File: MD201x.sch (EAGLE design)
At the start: 103 parts, among them IC1 78L05F, IC2 LM321MF, J1 8P8C-LED, J4 MA04-2, J5 MA05-2, J6 MA02-2, Q1 N-MOSFET-, Q2 N-MOSFET-, Q3 N-MOSFET-, Q4 N-MOSFET-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

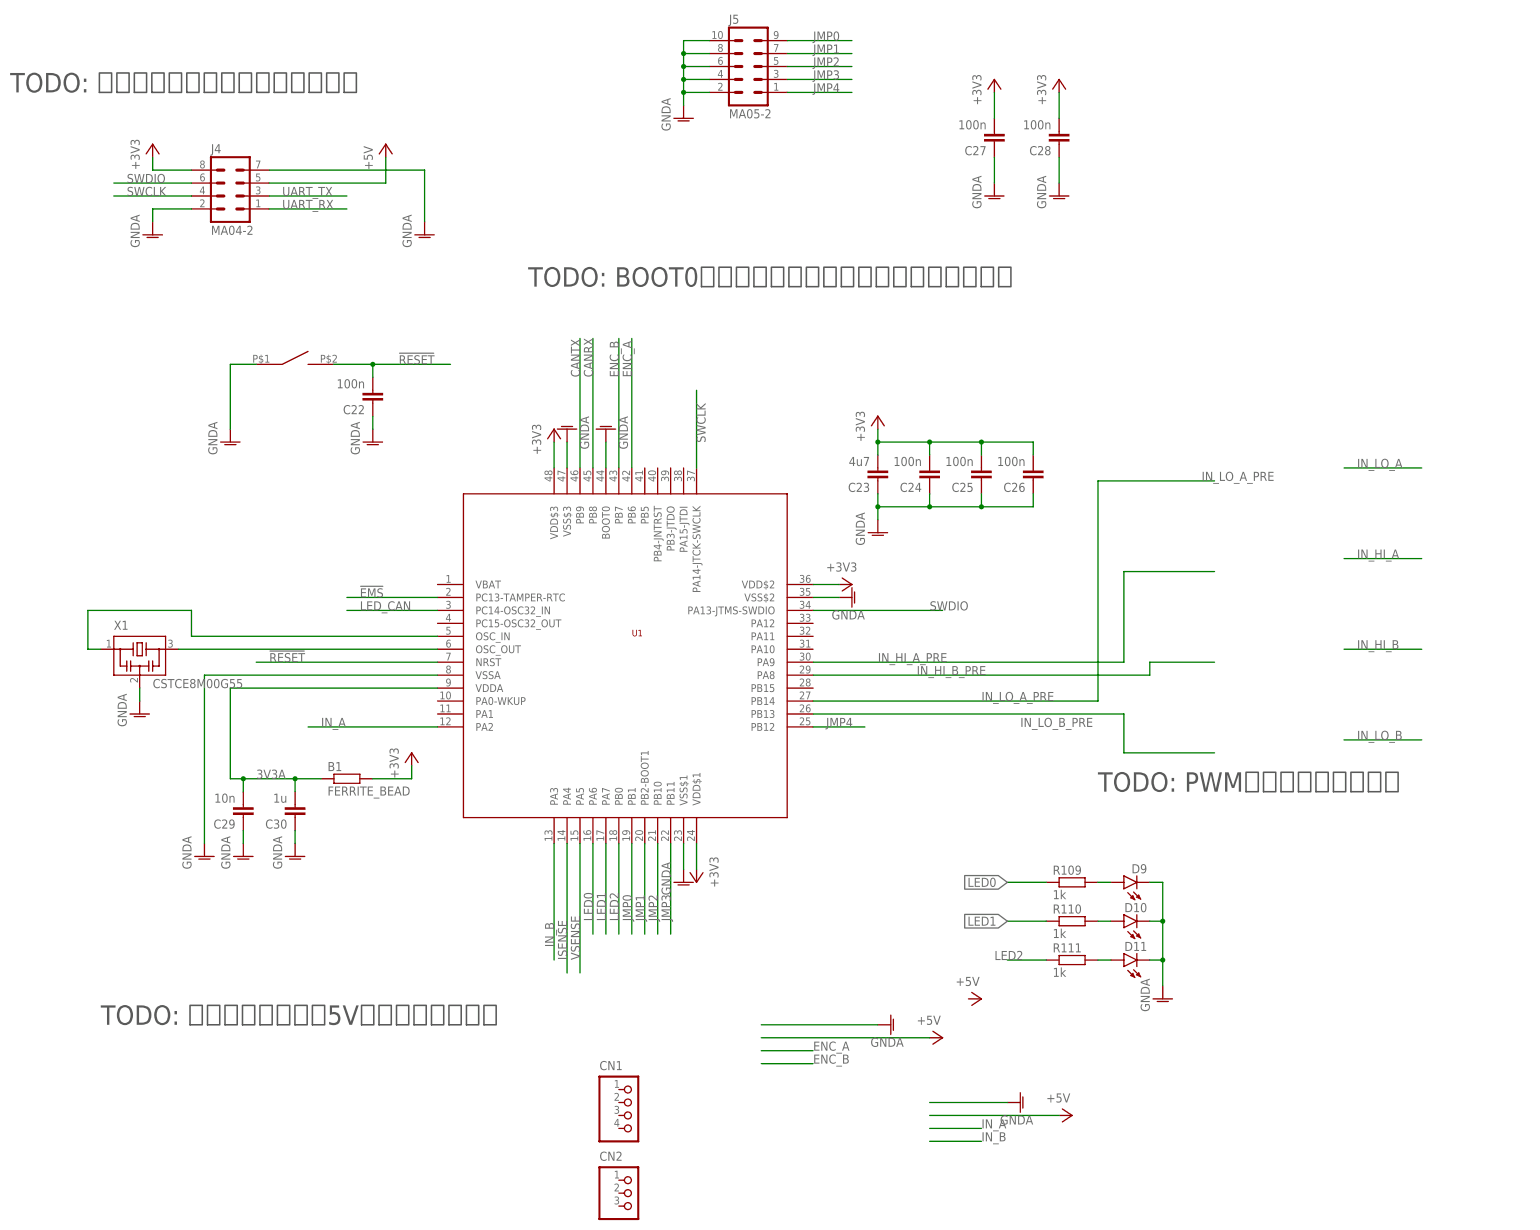
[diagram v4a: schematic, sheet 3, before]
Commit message: change: board size to 50x100, back-to-back MOSFETs
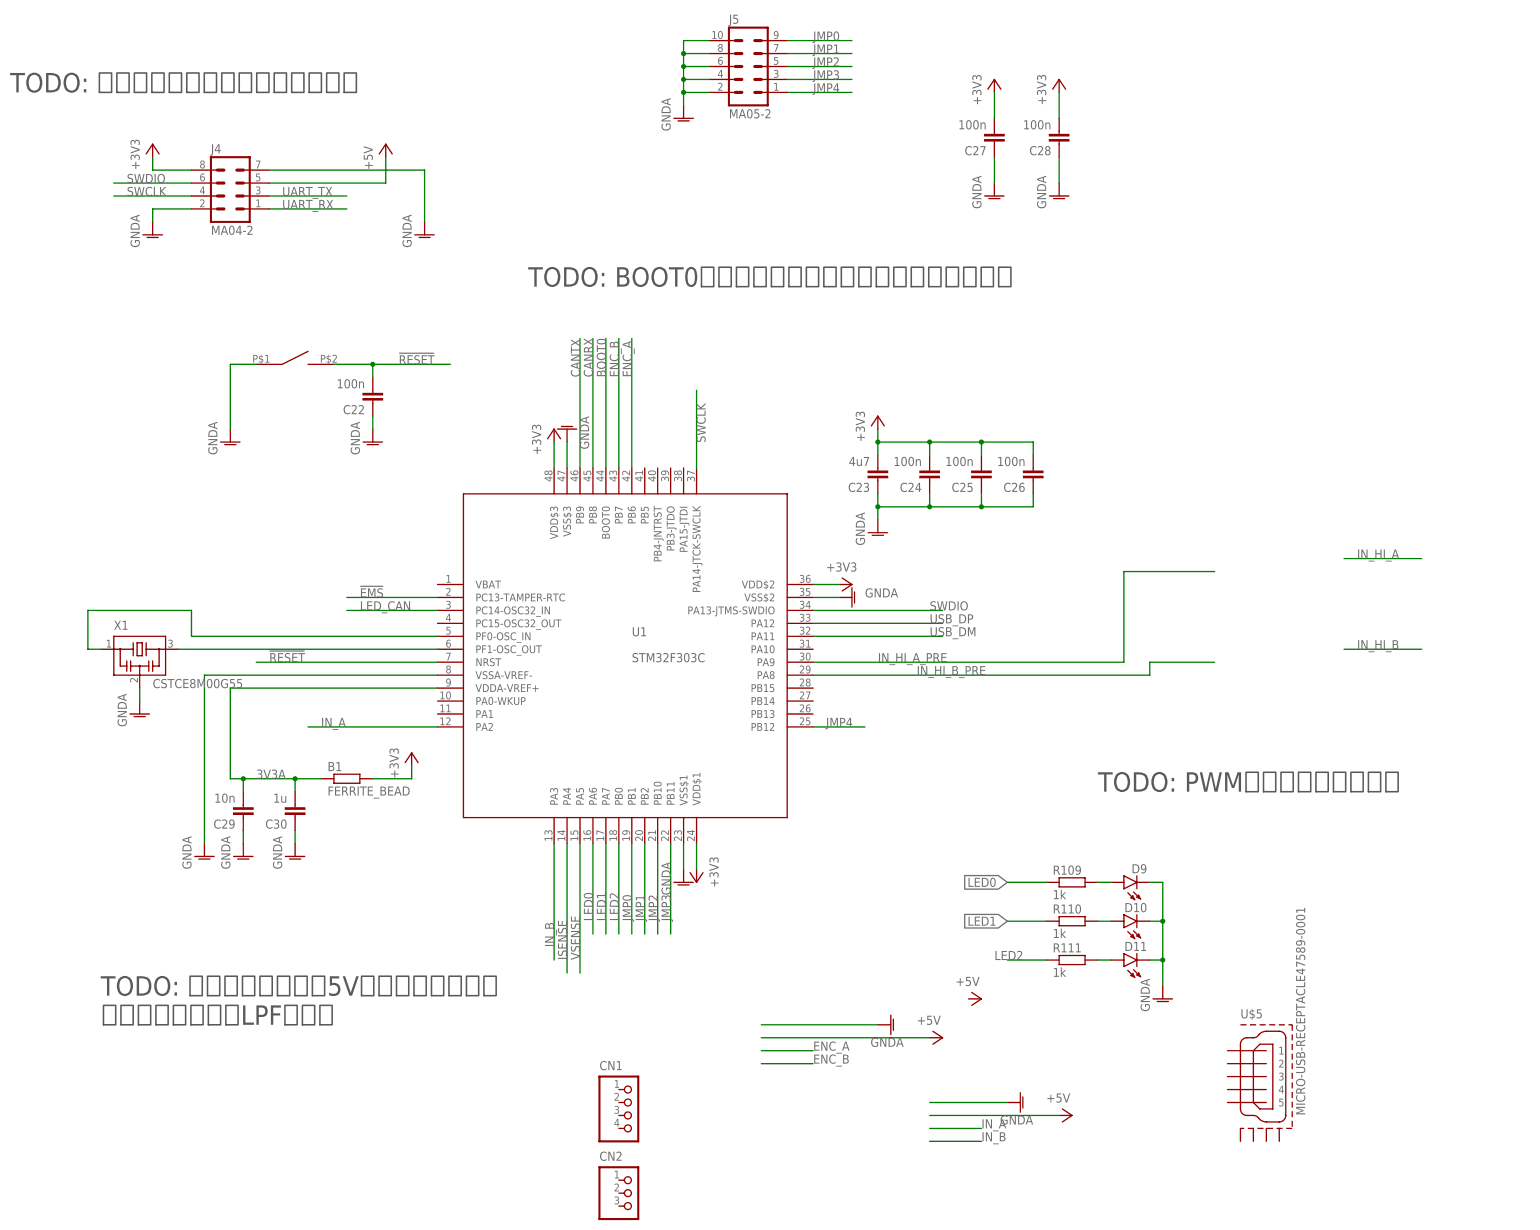
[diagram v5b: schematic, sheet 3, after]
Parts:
- added D4: BAS16W, diode:DIODE-SOD323-R
- added U$5: MICRO-USB-RECEPTACLE47589-0001, con-molex-usb:MICRO-USB-RECEPTACLE47589-0001
- U1: value STM32F103C8 -> STM32F303C; device stm32_mcu:STM32F103C8 -> stm32_mcu:STM32F303C
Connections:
- removed net IN_LO_A_PRE: U1.PB14
- removed net IN_LO_B_PRE: U1.PB13
- new net BOOT0: U1.BOOT0
- new net USB_DM: U1.PA11
- new net USB_DP: U1.PA12
- net 3V3A: now also U1.VDDA-VREF+; no longer U1.VDDA
- net GNDA: now also U1.VSSA-VREF-; no longer U1.BOOT0, U1.VSSA
- net JMP1: now also U1.PB2; no longer U1.PB2-BOOT1
- net N$10: now also U1.PF1-OSC_OUT; no longer U1.OSC_OUT
- net N$19: now also U1.PF0-OSC_IN; no longer U1.OSC_IN
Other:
- note added: "DFNのATA6560/1に変えたい"
- note added: "TODO: エンコーダ入力を5Vトレラントにする エンコーダ入力にLPF入れる"
- note removed: "TODO: エンコーダ入力を5Vトレラントにする"
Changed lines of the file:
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@@
 <?xml version="1.0" encoding="utf-8"?>
 <!DOCTYPE eagle SYSTEM "eagle.dtd">
-<eagle version="9.4.2">
+<eagle version="9.5.2">
 <drawing>
 <settings>
@@
 <part name="R20" library="rcl" library_urn="urn:adsk.eagle:library:334" deviceset="R-EU_" device="R0603" package3d_urn="urn:adsk.eagle:package:23555/3" value="4k7"/>
 <part name="R21" library="rcl" library_urn="urn:adsk.eagle:library:334" deviceset="R-EU_" device="R0603" package3d_urn="urn:adsk.eagle:package:23555/3" value="470"/>
-<part name="U1" library="stm32_mcu" deviceset="STM32F103C8" device=""/>
+<part name="U1" library="stm32_mcu" deviceset="STM32F303C*" device=""/>
 <part name="P+12" library="supply1" library_urn="urn:adsk.eagle:library:371" deviceset="+3V3" device=""/>
 <part name="P+19" library="supply1" library_urn="urn:adsk.eagle:library:371" deviceset="+3V3" device=""/>
@@
 <part name="GND13" library="supply1" library_urn="urn:adsk.eagle:library:371" deviceset="GNDA" device=""/>
 <part name="GND14" library="supply1" library_urn="urn:adsk.eagle:library:371" deviceset="GNDA" device=""/>
-<part name="GND15" library="supply1" library_urn="urn:adsk.eagle:library:371" deviceset="GNDA" device=""/>
 <part name="GND16" library="supply1" library_urn="urn:adsk.eagle:library:371" deviceset="GNDA" device=""/>
 <part name="GND24" library="supply1" library_urn="urn:adsk.eagle:library:371" deviceset="GNDA" device=""/>
@@
 <part name="C31" library="rcl" library_urn="urn:adsk.eagle:library:334" deviceset="C-EU" device="C0603" package3d_urn="urn:adsk.eagle:package:23616/2"/>
 <part name="U$4" library="lib_ysk" deviceset="DGD05473" device="FN" package3d_urn="urn:adsk.eagle:package:12826382/1"/>
+<part name="U$5" library="con-molex-usb" deviceset="MICRO-USB-RECEPTACLE" device="47589-0001"/>
+<part name="D4" library="diode" library_urn="urn:adsk.eagle:library:210" deviceset="DIODE-" device="SOD323-R" package3d_urn="urn:adsk.eagle:package:43437/1" value="BAS16W"/>
 </parts>
 <sheets>
@@
 </instance>
 <instance part="U$4" gate="G$1" x="12.7" y="27.94" smashed="yes"/>
+<instance part="D4" gate="G$1" x="40.64" y="106.68" smashed="yes" rot="R90">
+<attribute name="NAME" x="40.1574" y="109.22" size="1.778" layer="95" rot="R90"/>
+<attribute name="VALUE" x="42.9514" y="109.22" size="1.778" layer="96" rot="R90"/>
+</instance>
 </instances>
 <busses>
@@
 <sheet>
 <plain>
+<text x="-17.78" y="99.06" size="3.81" layer="97">DFNのATA6560/1に変えたい</text>
 </plain>
 <instances>
@@
 <text x="96.52" y="127" size="3.81" layer="97">TODO: BOOT0をジャンパで切り替えられるようにする</text>
 <text x="-5.08" y="165.1" size="3.81" layer="97">TODO: デバッガ用コネクタを最適化する</text>
-<text x="12.7" y="-17.78" size="3.81" layer="97">TODO: エンコーダ入力を5Vトレラントにする</text>
+<text x="12.7" y="-17.78" size="3.81" layer="97">TODO: エンコーダ入力を5Vトレラントにする
+エンコーダ入力にLPF入れる</text>
 <text x="208.28" y="27.94" size="3.81" layer="97">TODO: PWM信号を直列終端する</text>
 </plain>
 <instances>
 <instance part="U1" gate="G$1" x="114.3" y="55.88" smashed="yes">
-<attribute name="NAME" x="116.84" y="58.42" size="1.27" layer="94"/>
+<attribute name="NAME" x="116.84" y="58.42" size="1.778" layer="95"/>
+<attribute name="VALUE" x="116.84" y="53.34" size="1.778" layer="96"/>
 </instance>
 <instance part="P+12" gate="G$1" x="160.02" y="68.58" smashed="yes" rot="R270">
@@
 </instance>
 <instance part="GND14" gate="1" x="160.02" y="66.04" smashed="yes" rot="R90">
-<attribute name="VALUE" x="162.56" y="63.5" size="1.778" layer="96" rot="R180"/>
-</instance>
-<instance part="GND15" gate="1" x="111.76" y="99.06" smashed="yes" rot="R180">
-<attribute name="VALUE" x="114.3" y="101.6" size="1.778" layer="96" rot="R270"/>
+<attribute name="VALUE" x="162.56" y="66.04" size="1.778" layer="96"/>
 </instance>
 <instance part="GND16" gate="1" x="104.14" y="99.06" smashed="yes" rot="R180">
@@
 <attribute name="NAME" x="110.49" y="-44.45" size="1.778" layer="95"/>
 <attribute name="VALUE" x="110.49" y="-58.42" size="1.778" layer="96"/>
+</instance>
+<instance part="U$5" gate="G$1" x="238.76" y="-27.94" smashed="yes">
+<attribute name="NAME" x="236.22" y="-16.51" size="1.778" layer="95" font="vector"/>
+<attribute name="VALUE" x="248.92" y="-35.56" size="1.778" layer="96" font="vector" rot="R90"/>
 </instance>
 </instances>
@@
 <net name="N$10" class="0">
 <segment>
-<pinref part="U1" gate="G$1" pin="OSC_OUT"/>
+<pinref part="U1" gate="G$1" pin="PF1-OSC_OUT"/>
 <wire x1="27.94" y1="55.88" x2="78.74" y2="55.88" width="0.1524" layer="91"/>
 <pinref part="X1" gate="G$1" pin="3"/>
@@
 <wire x1="10.16" y1="55.88" x2="10.16" y2="63.5" width="0.1524" layer="91"/>
 <wire x1="10.16" y1="63.5" x2="30.48" y2="63.5" width="0.1524" layer="91"/>
-<pinref part="U1" gate="G$1" pin="OSC_IN"/>
+<pinref part="U1" gate="G$1" pin="PF0-OSC_IN"/>
 <wire x1="30.48" y1="63.5" x2="30.48" y2="58.42" width="0.1524" layer="91"/>
 <wire x1="30.48" y1="58.42" x2="78.74" y2="58.42" width="0.1524" layer="91"/>
@@
 </segment>
 <segment>
-<pinref part="U1" gate="G$1" pin="VSSA"/>
+<pinref part="U1" gate="G$1" pin="VSSA-VREF-"/>
 <wire x1="33.02" y1="17.78" x2="33.02" y2="50.8" width="0.1524" layer="91"/>
 <wire x1="33.02" y1="50.8" x2="78.74" y2="50.8" width="0.1524" layer="91"/>
@@
 <wire x1="157.48" y1="66.04" x2="152.4" y2="66.04" width="0.1524" layer="91"/>
 <pinref part="GND14" gate="1" pin="GNDA"/>
-</segment>
-<segment>
-<pinref part="U1" gate="G$1" pin="BOOT0"/>
-<wire x1="111.76" y1="96.52" x2="111.76" y2="91.44" width="0.1524" layer="91"/>
-<pinref part="GND15" gate="1" pin="GNDA"/>
 </segment>
 <segment>
@@
 <net name="3V3A" class="0">
 <segment>
-<pinref part="U1" gate="G$1" pin="VDDA"/>
+<pinref part="U1" gate="G$1" pin="VDDA-VREF+"/>
 <wire x1="50.8" y1="30.48" x2="40.64" y2="30.48" width="0.1524" layer="91"/>
 <wire x1="40.64" y1="30.48" x2="38.1" y2="30.48" width="0.1524" layer="91"/>
@@
 </segment>
 </net>
-<net name="IN_LO_A" class="0">
-<segment>
-<wire x1="256.54" y1="91.44" x2="271.78" y2="91.44" width="0.1524" layer="91"/>
-<label x="259.08" y="91.44" size="1.778" layer="95"/>
-</segment>
-</net>
-<net name="IN_LO_B" class="0">
-<segment>
-<wire x1="256.54" y1="38.1" x2="271.78" y2="38.1" width="0.1524" layer="91"/>
-<label x="259.08" y="38.1" size="1.778" layer="95"/>
-</segment>
-</net>
 <net name="IN_A" class="0">
 <segment>
@@
 </segment>
 </net>
-<net name="IN_LO_A_PRE" class="0">
-<segment>
-<pinref part="U1" gate="G$1" pin="PB14"/>
-<wire x1="152.4" y1="45.72" x2="208.28" y2="45.72" width="0.1524" layer="91"/>
-<label x="185.42" y="45.72" size="1.778" layer="95"/>
-<label x="228.6" y="88.9" size="1.778" layer="95"/>
-<wire x1="231.14" y1="88.9" x2="208.28" y2="88.9" width="0.1524" layer="91"/>
-<wire x1="208.28" y1="88.9" x2="208.28" y2="45.72" width="0.1524" layer="91"/>
-</segment>
-</net>
-<net name="IN_LO_B_PRE" class="0">
-<segment>
-<pinref part="U1" gate="G$1" pin="PB13"/>
-<label x="193.04" y="40.64" size="1.778" layer="95"/>
-<wire x1="152.4" y1="43.18" x2="213.36" y2="43.18" width="0.1524" layer="91"/>
-<wire x1="213.36" y1="43.18" x2="213.36" y2="35.56" width="0.1524" layer="91"/>
-<wire x1="213.36" y1="35.56" x2="231.14" y2="35.56" width="0.1524" layer="91"/>
-</segment>
-</net>
 <net name="JMP0" class="0">
 <segment>
@@
 <net name="JMP1" class="0">
 <segment>
-<pinref part="U1" gate="G$1" pin="PB2-BOOT1"/>
+<pinref part="U1" gate="G$1" pin="PB2"/>
 <wire x1="119.38" y1="17.78" x2="119.38" y2="0" width="0.1524" layer="91"/>
 <label x="119.38" y="2.54" size="1.778" layer="95" rot="R90"/>
@@
 <pinref part="U1" gate="G$1" pin="PA5"/>
 <label x="106.68" y="-5.08" size="1.778" layer="95" rot="R90"/>
+</segment>
+</net>
+<net name="BOOT0" class="0">
+<segment>
+<pinref part="U1" gate="G$1" pin="BOOT0"/>
+<wire x1="111.76" y1="116.84" x2="111.76" y2="91.44" width="0.1524" layer="91"/>
+<label x="111.76" y="109.22" size="1.778" layer="95" rot="R90"/>
+</segment>
+</net>
+<net name="USB_DM" class="0">
+<segment>
+<pinref part="U1" gate="G$1" pin="PA11"/>
+<wire x1="152.4" y1="58.42" x2="177.8" y2="58.42" width="0.1524" layer="91"/>
+<label x="175.26" y="58.42" size="1.778" layer="95"/>
+</segment>
+</net>
+<net name="USB_DP" class="0">
+<segment>
+<pinref part="U1" gate="G$1" pin="PA12"/>
+<wire x1="152.4" y1="60.96" x2="177.8" y2="60.96" width="0.1524" layer="91"/>
+<label x="175.26" y="60.96" size="1.778" layer="95"/>
 </segment>
 </net>
@@
 </drawing>
 <compatibility>
+<note version="6.3" minversion="6.2.2" severity="warning">
+Since Version 6.2.2 text objects can contain more than one line,
+which will not be processed correctly with this version.
+</note>
 <note version="8.2" severity="warning">
 Since Version 8.2, EAGLE supports online libraries. The ids
